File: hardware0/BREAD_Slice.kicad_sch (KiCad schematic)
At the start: 19 parts, among them J1 I2C_01x04, J2 Conn_01x10_Female, J3 Conn_01x02_Socket, J4 Conn_01x02_Socket, J5 Conn_01x02_Socket, J6 Conn_01x02_Socket

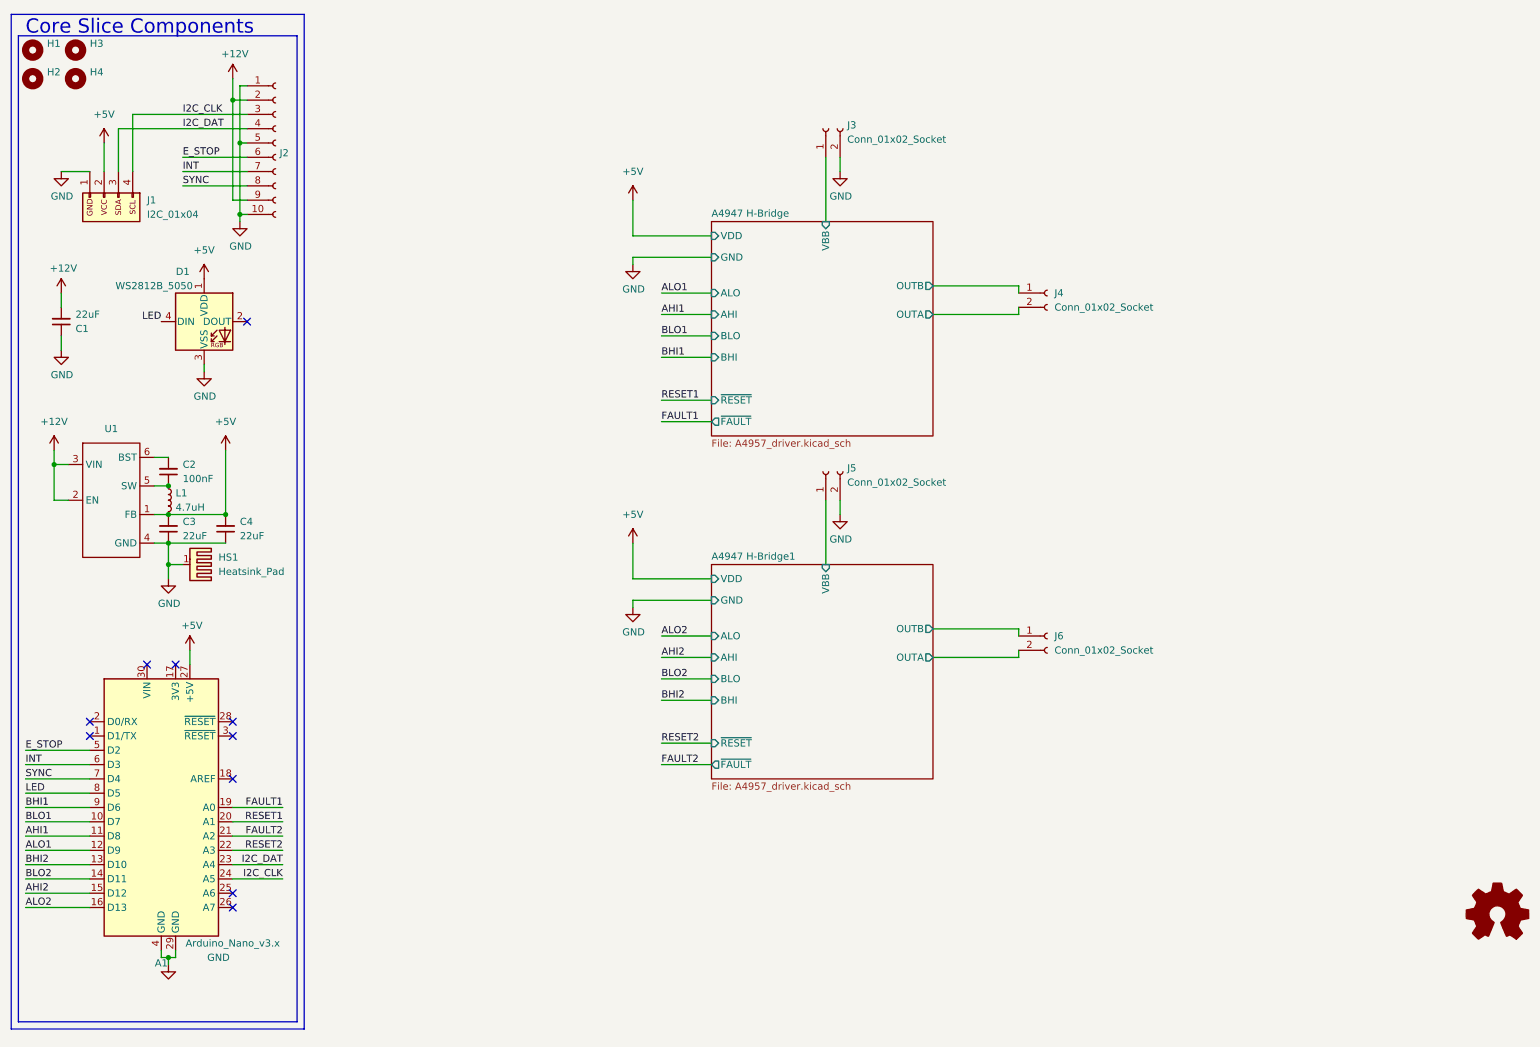
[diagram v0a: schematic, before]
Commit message: initial layout poisitions done
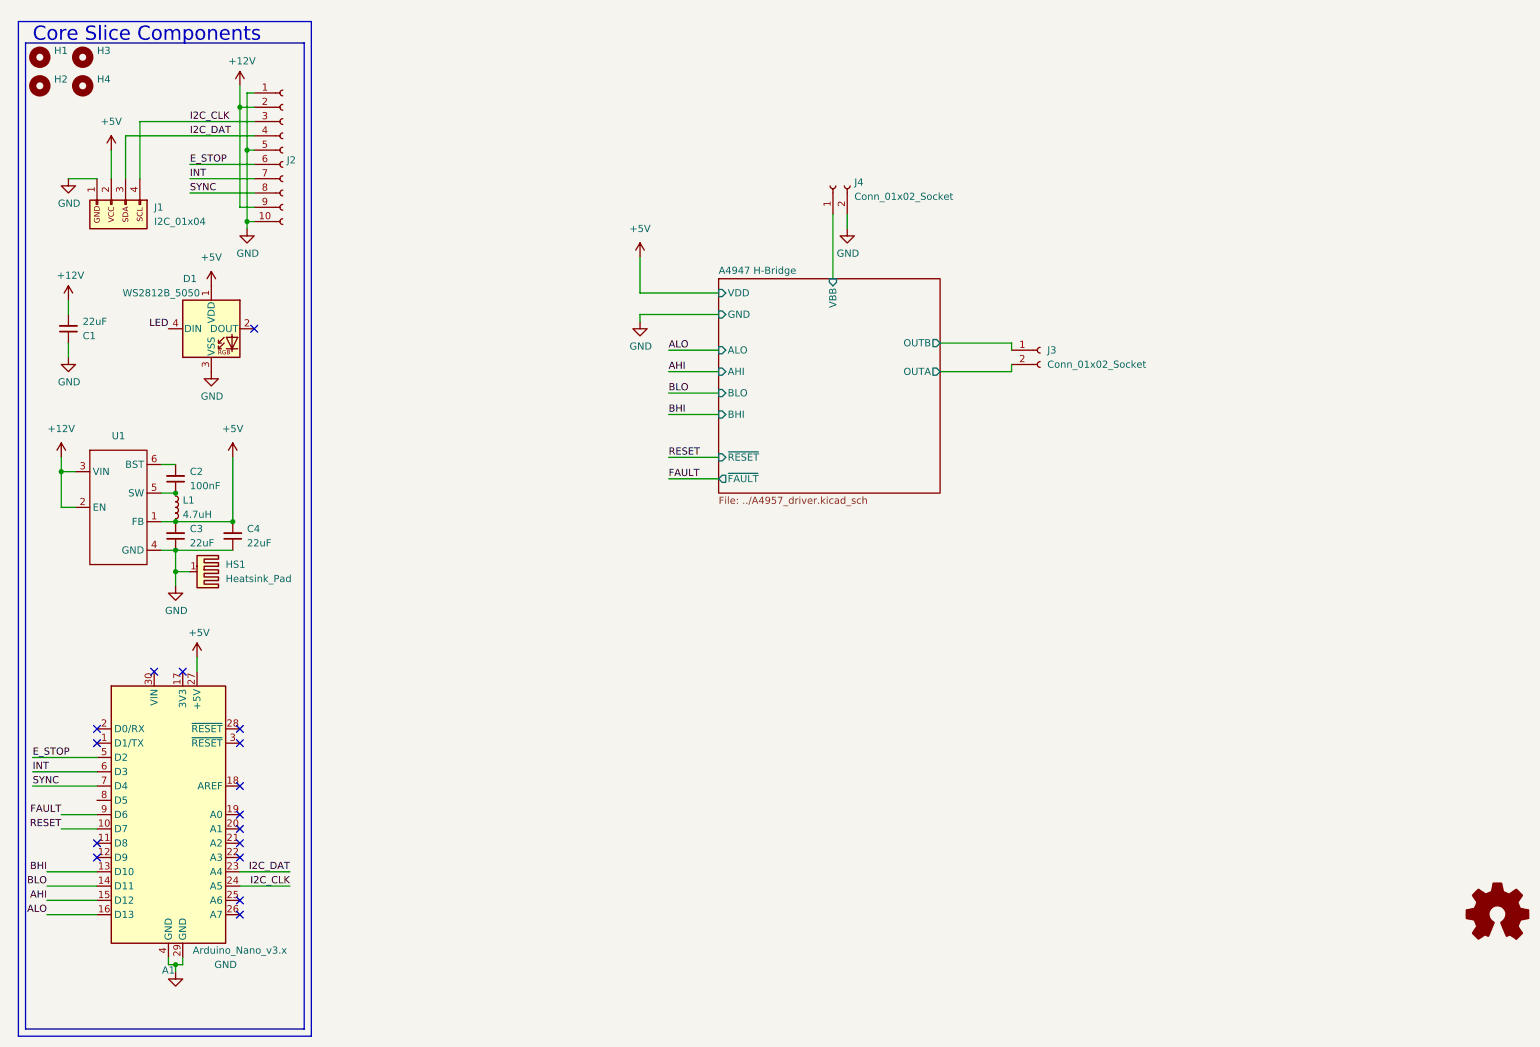
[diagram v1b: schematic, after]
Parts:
- removed J5, J6: Conn_01x02_Socket, Library:Term_Block_1x2_P10.16mm, symbol Connector:Conn_01x02_Socket
- added Logo1: Logo_Open_Hardware_Small, Symbol:OSHW-Symbol_6.7x6mm_SilkScreen, symbol Graphic:Logo_Open_Hardware_Small
- HS1: footprint KML-Custom:Thermal Pad -> SparkFun-Fuse:Thermal Pad
- J3, J4: footprint Library:Term_Block_1x2_P10.16mm -> (none)
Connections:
- net A4947 H-Bridge/OUTA: now also J3.2 (Pin_2); no longer J4.2 (Pin_2)
- net A4947 H-Bridge/OUTB: now also J3.1 (Pin_1); no longer J4.1 (Pin_1)
- net A4947 H-Bridge/VBB: now also J4.1 (Pin_1); no longer J3.1 (Pin_1)
- net GND: now also J4.2 (Pin_2); no longer J3.2 (Pin_2)
- net LED: no longer A1.8 (D5)
- net AHI1: no longer names the net of A1.11 (D8)
- net AHI2 renamed AHI
- net ALO1: no longer names the net of A1.12 (D9)
- net ALO2 renamed ALO
- net BHI1 renamed FAULT
- net BHI2 renamed BHI
- net BLO1 renamed RESET
- net BLO2 renamed BLO
- net FAULT1: no longer names the net of A1.19 (A0)
- net FAULT2: no longer names the net of A1.21 (A2)
- net RESET1: no longer names the net of A1.20 (A1)
- net RESET2: no longer names the net of A1.22 (A3)
- no-connect marks 10 -> 16
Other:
- removed sheet A4947 H-Bridge1
- sheet A4947 H-Bridge: file A4957_driver.kicad_sch -> ../A4957_driver.kicad_sch
